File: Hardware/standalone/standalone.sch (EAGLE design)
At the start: 98 parts, among them IC1 STM32F050C6T6A, IC2 AP1212, IC3 IR2104S, Q1 32.768kHz, U10 ZXCT1107SA-7, U11 NMOS_2N7002, U12 NMOS_2N7002, U2 FDS6690a, U3 FDS6690a, U4 LM2576S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

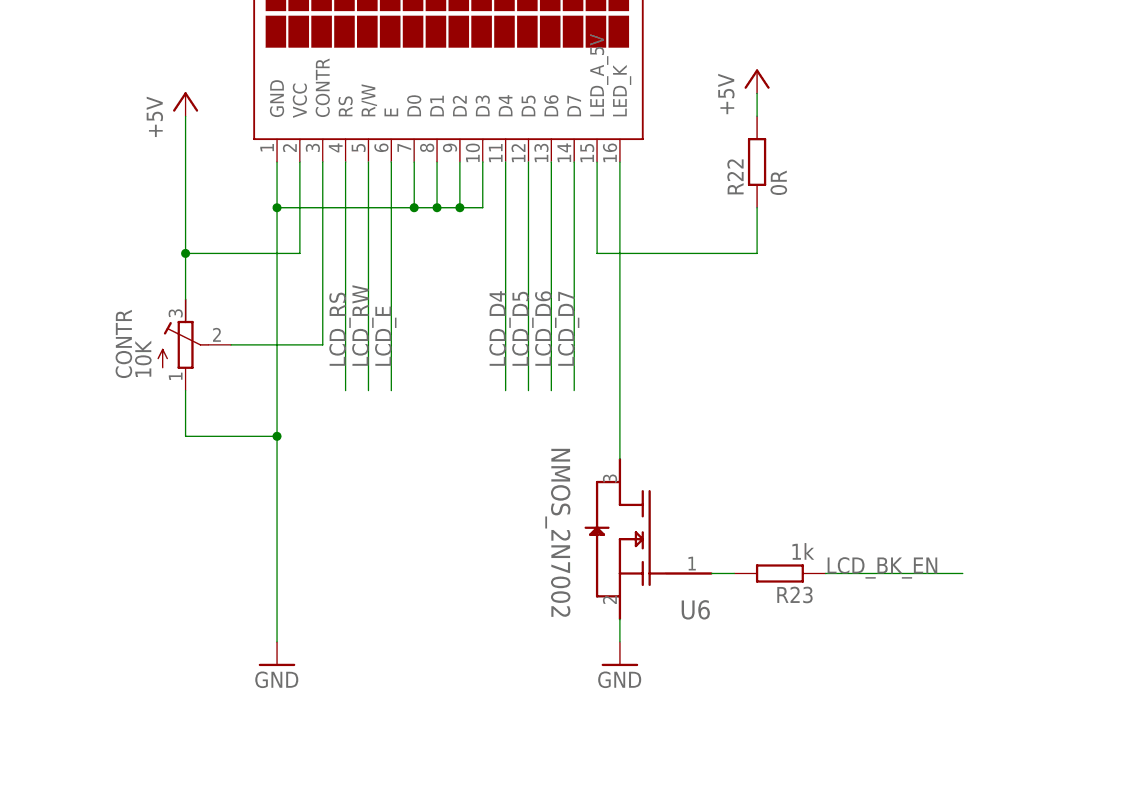
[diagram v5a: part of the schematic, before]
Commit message: izuba.box home production data added
This production data will be used to obtain a quote for assembly from
quick-tech.
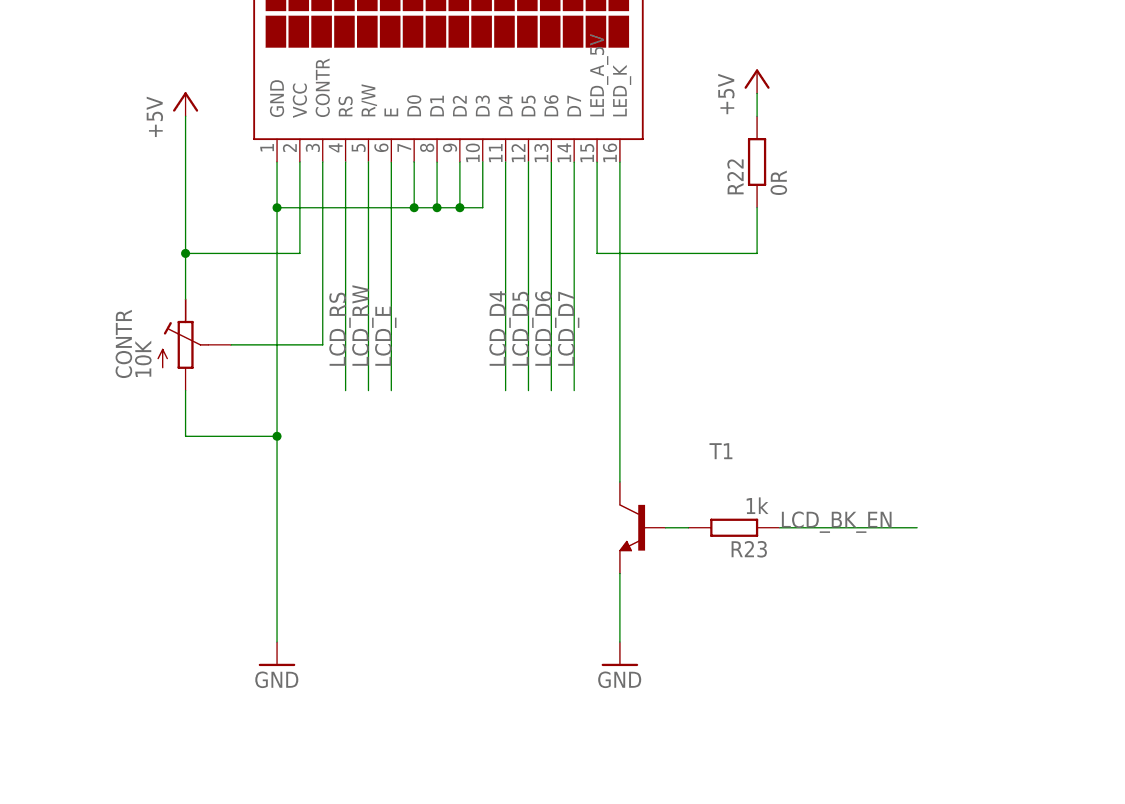
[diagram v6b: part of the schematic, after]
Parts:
- removed U6: NMOS_2N7002, equinox:NMOS_2N7002
- added T1: (no value), transistor:BC847B-NPN-SOT23-BEC
- CONTR: device resistor:R-TRIMM3304W -> equinox:R_TRIMM_TC33X
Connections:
- net GND: now also T1.E; no longer U6.S
- net N$31: now also T1.C; no longer U6.D
- net N$32: now also T1.B; no longer U6.G
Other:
- note added: "TODO: -"
- note removed: "TODO: - Contrast Adjust Pot needs changing - Swap MOS with BJT - Change XTAL to new 6pF"
- moved on the sheet: R23
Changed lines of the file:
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@@
 </variantdefs>
 <classes>
-<class number="0" name="default" width="0.381" drill="0.6096">
-<clearance class="0" value="0.381"/>
+<class number="0" name="default" width="0.381" drill="0.6">
+<clearance class="0" value="0.254"/>
 </class>
-<class number="1" name="pwr" width="0.02580625" drill="0.6096">
-<clearance class="1" value="0.508"/>
+<class number="1" name="pwr" width="0.381" drill="0.6">
+<clearance class="1" value="0.381"/>
 </class>
-<class number="2" name="pow_12v" width="1.3716" drill="0.762">
-<clearance class="2" value="0.508"/>
+<class number="2" name="pow_12v" width="0.381" drill="0.6">
+<clearance class="2" value="0.381"/>
 </class>
-<class number="3" name="gnd" width="0.508" drill="0.6096">
+<class number="3" name="gnd" width="0.381" drill="0.6">
 </class>
 </classes>
@@
 <part name="R20" library="rcl" deviceset="R-EU_" device="M0805" value="1k"/>
 <part name="P+5" library="supply1" deviceset="+5V" device=""/>
-<part name="CONTR" library="resistor" deviceset="R-TRIMM" device="3304W" value="10K"/>
-<part name="U6" library="equinox" deviceset="NMOS_2N7002" device="">
-<attribute name="MPN" value="2N7002-7-F"/>
-<attribute name="OC_FARNELL" value="1713823"/>
-<attribute name="OC_NEWARK" value="25R5679"/>
-<attribute name="PACKAGE" value="SOT-23-3"/>
-<attribute name="SUPPLIER" value="DIODES INC."/>
-</part>
+<part name="CONTR" library="equinox" deviceset="R_TRIMM_TC33X" device="" value="10K"/>
 <part name="R22" library="resistor" deviceset="R-EU_" device="M0805" value="0R"/>
 <part name="R23" library="resistor" deviceset="R-EU_" device="M0805" value="1k"/>
@@
 <attribute name="OC_FARNELL" value="1712823"/>
 <attribute name="OC_NEWARK" value="-"/>
+</part>
+<part name="T1" library="transistor" deviceset="*-NPN-" device="SOT23-BEC" technology="BC847B">
+<attribute name="OC_FARNELL" value="1081232   "/>
 </part>
 </parts>
@@
 <text x="406.4" y="513.08" size="6.4516" layer="94" font="vector">NOTES</text>
 <text x="406.4" y="502.92" size="3.81" layer="98" rot="MR180">TODO:
-  - Contrast Adjust Pot needs changing
-  - Swap MOS with BJT
-  - Change XTAL to new 6pF</text>
+  - </text>
 <text x="662.94" y="127" size="1.778" layer="98">0.5A Current Limit</text>
 <text x="662.94" y="86.36" size="1.778" layer="98">0.5A Current Limit</text>
@@
 <instance part="R20" gate="G$1" x="642.62" y="170.18"/>
 <instance part="P+5" gate="1" x="342.9" y="228.6"/>
-<instance part="CONTR" gate="G$1" x="279.4" y="198.12"/>
-<instance part="U6" gate="A" x="330.2" y="177.8" rot="MR0"/>
+<instance part="CONTR" gate="R1" x="279.4" y="198.12"/>
 <instance part="R22" gate="G$1" x="342.9" y="218.44" rot="R90"/>
-<instance part="R23" gate="G$1" x="345.44" y="172.72" rot="R180"/>
+<instance part="R23" gate="G$1" x="340.36" y="177.8" rot="R180"/>
 <instance part="JTAG" gate="A" x="30.48" y="215.9" rot="MR0"/>
 <instance part="+3V8" gate="G$1" x="63.5" y="228.6"/>
@@
 <attribute name="NAME" x="128.016" y="147.32" size="1.778" layer="95" rot="R270"/>
 <attribute name="VALUE" x="121.92" y="157.48" size="1.778" layer="96" rot="R270"/>
+</instance>
+<instance part="T1" gate="G$1" x="330.2" y="177.8" rot="MR0">
+<attribute name="OC_FARNELL" x="330.2" y="177.8" size="1.778" layer="96" rot="MR0" display="off"/>
 </instance>
 </instances>
@@
 <wire x1="279.4" y1="208.28" x2="292.1" y2="208.28" width="0.1524" layer="91"/>
 <wire x1="292.1" y1="208.28" x2="292.1" y2="218.44" width="0.1524" layer="91"/>
-<pinref part="CONTR" gate="G$1" pin="A"/>
+<pinref part="CONTR" gate="R1" pin="A"/>
 <wire x1="279.4" y1="203.2" x2="279.4" y2="208.28" width="0.1524" layer="91"/>
 <junction x="279.4" y="208.28"/>
@@
 <wire x1="294.64" y1="218.44" x2="294.64" y2="198.12" width="0.1524" layer="91"/>
 <wire x1="294.64" y1="198.12" x2="284.48" y2="198.12" width="0.1524" layer="91"/>
-<pinref part="CONTR" gate="G$1" pin="S"/>
+<pinref part="CONTR" gate="R1" pin="S"/>
 </segment>
 </net>
@@
 <segment>
 <pinref part="DIS1" gate="G$1" pin="LED_K"/>
-<pinref part="U6" gate="A" pin="D"/>
-<wire x1="327.66" y1="185.42" x2="327.66" y2="218.44" width="0.1524" layer="91"/>
+<wire x1="327.66" y1="182.88" x2="327.66" y2="218.44" width="0.1524" layer="91"/>
+<pinref part="T1" gate="G$1" pin="C"/>
 </segment>
 </net>
 <net name="N$32" class="0">
 <segment>
-<pinref part="U6" gate="A" pin="G"/>
 <pinref part="R23" gate="G$1" pin="2"/>
-<wire x1="337.82" y1="172.72" x2="340.36" y2="172.72" width="0.1524" layer="91"/>
+<wire x1="332.74" y1="177.8" x2="335.28" y2="177.8" width="0.1524" layer="91"/>
+<pinref part="T1" gate="G$1" pin="B"/>
 </segment>
 </net>
@@
 <segment>
 <pinref part="R23" gate="G$1" pin="1"/>
-<wire x1="350.52" y1="172.72" x2="365.76" y2="172.72" width="0.1524" layer="91"/>
-<label x="350.52" y="172.72" size="1.778" layer="95"/>
+<wire x1="345.44" y1="177.8" x2="360.68" y2="177.8" width="0.1524" layer="91"/>
+<label x="345.44" y="177.8" size="1.778" layer="95"/>
 </segment>
 <segment>
@@
 <segment>
 <pinref part="GND1" gate="1" pin="GND"/>
-<pinref part="U6" gate="A" pin="S"/>
-<wire x1="327.66" y1="165.1" x2="327.66" y2="167.64" width="0.1524" layer="91"/>
+<pinref part="T1" gate="G$1" pin="E"/>
+<wire x1="327.66" y1="165.1" x2="327.66" y2="172.72" width="0.1524" layer="91"/>
 </segment>
 <segment>
@@
 <segment>
 <pinref part="GND30" gate="1" pin="GND"/>
-<pinref part="CONTR" gate="G$1" pin="E"/>
+<pinref part="CONTR" gate="R1" pin="E"/>
 <wire x1="279.4" y1="193.04" x2="279.4" y2="187.96" width="0.1524" layer="91"/>
 <pinref part="DIS1" gate="G$1" pin="GND"/>
